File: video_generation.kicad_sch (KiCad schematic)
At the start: 49 parts, among them J12 28L22, J13 74LS86, J14 74LS166, J15 74LS161, K0000 74LS00, K10 74LS08, K11 74LS273, K12 74LS273, K14 74LS10, K15 74LS04, U14 74LS00, U2 74LS32, U3 74LS08, U4 74LS04, U5 74LS00

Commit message: video gen and memory: wire renaming, but something is still missing
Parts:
- added TP1: EXT, symbol Connector:TestPoint_Alt
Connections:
- net cl4 is gone; now on net ra4: E7E11.34 (RA4)
- net ~{BEAM} is gone; now on net BEAM: J?.5 (Pin_5)
- net GND: now also E12.8 (GND), H12H14.12 (GND), K11.10 (GND), K12.10 (GND), L10.8 (GND)
- net VCC: now also E12.1 (~{Mr}), E12.16 (VCC), H12H14.24 (VCC), K11.20 (VCC), K12.20 (VCC), L10.16 (VCC), R67.1
- net char0: now also H11.16 (Q6); no longer H11.2 (Q0)
- net char1: now also H11.2 (Q0); no longer H11.5 (Q1)
- net char2: now also H11.19 (Q7); no longer H11.6 (Q2)
- net char3: now also H11.12 (Q4); no longer H11.9 (Q3)
- net char4: now also H11.9 (Q3); no longer H11.12 (Q4)
- net char5: now also H11.6 (Q2); no longer H11.15 (Q5)
- net char6: now also H11.15 (Q5); no longer H11.16 (Q6)
- net char7: now also H11.5 (Q1); no longer H11.19 (Q7)
- net cl0: no longer E7E11.38 (RA0)
- net cl1: no longer E7E11.37 (RA1)
- net cl2: no longer E7E11.36 (RA2)
- net cl3: no longer E7E11.35 (RA3)
- net ra0: now reaches J12.1 (A0)
- net ra0: now also E7E11.38 (RA0)
- net ROM_D5: now reaches J12.12 (D5)
- net ROM_D5: now also K12.18 (D7)
- net ROM_D6: now reaches J12.13 (D6)
- net ROM_D6: now also K12.17 (D6)
- net ROM_D7: now reaches J12.14 (D7)
- net ROM_D7: now also K12.14 (D5)
- net ROM_A5: now reaches J12.17 (A5)
- net ROM_A5: now also K11.16 (Q6)
- net ROM_A6: now reaches J12.18 (A6)
- net ROM_A6: now also K11.19 (Q7)
- net ROM_A7: now reaches J12.19 (A7)
- net ROM_A7: now also K11.15 (Q5)
- net ra1: now reaches J12.2 (A1)
- net ra1: now also E7E11.37 (RA1)
- net ra2: now reaches J12.3 (A2)
- net ra2: now also E7E11.36 (RA2)
- net ra3: now reaches J12.4 (A3)
- net ra3: now also E7E11.35 (RA3)
- net ra4: now reaches J12.5 (A4)
- net A0: now reaches E7E11.24 (RS)
- net chmd3: now reaches H11.13 (D4)
- net chmd6: now reaches H11.14 (D5)
- net chmd0: now reaches H11.17 (D6)
- net chmd2: now reaches H11.18 (D7)
- net chmd1: now reaches H11.3 (D0)
- net chmd7: now reaches H11.4 (D1)
- net chmd5: now reaches H11.7 (D2)
- net chmd4: now reaches H11.8 (D3)
- net at K11.2 (Q0): now also TP1.1
- net 15MHzClock renamed PIXEL_CLK
- net MainClock renamed CRTC_CLK
- net attr_data0 renamed attrmd0
- net attr_data1 renamed attrmd1
- net attr_data2 renamed attrmd2
- net attr_data3 renamed attrmd3
- net attr_data4 renamed attrmd4
- net attr_data5 renamed attrmd5
- net attr_data6 renamed attrmd6
- net attr_data7 renamed attrmd7
- net data0 renamed D0
- net data1 renamed D1
- net data2 renamed D2
- net data3 renamed D3
- net data4 renamed D4
- net data5 renamed D5
- net data6 renamed D6
- net data7 renamed D7
- net ma0 renamed VMA0
- net ma1 renamed VMA1
- net ma10 renamed VMA10
- net ma2 renamed VMA2
- net ma3 renamed VMA3
- net ma4 renamed VMA4
- net ma5 renamed VMA5
- net ma6 renamed VMA6
- net ma7 renamed VMA7
- net ma8 renamed VMA8
- net ma9 renamed VMA9
- net ~{MainClock} renamed ~{CRTC_CLK}
- net ~{TC} renamed ~{PIXEL_EN}
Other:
- note added: "Attribute Memory Data"
- note added: "Character Memory Data"
- note added: "Raster address"
- note added: "TODO"
- note added: "Video memory Address"
- note removed: "D2 from attribute RAM is something related to cursor"
- note removed: "EXT pad"
- note removed: "NOTE:SWAP"
- note removed: "NOTE:SWAP: actual routing on board differs due to physical constraints, but functionality is the same."
- note removed: "ROM_A5"
- note removed: "ROM_A6"
- note removed: "ROM_A7"
- note removed: "ROM_D5"
- note removed: "ROM_D6"
- note removed: "ROM_D7"
- note removed: "VERIFY"
- note removed: "registered ATTR RAM D0"
- note removed: "registered ATTR RAM D1"
- note removed: "registered D2 attr ram"
- note removed: "registered D5 ROM"
- note removed: "registered D6 ROM"
- note removed: "registered D7 ROM"
- moved on the sheet: K10B, R42, R67

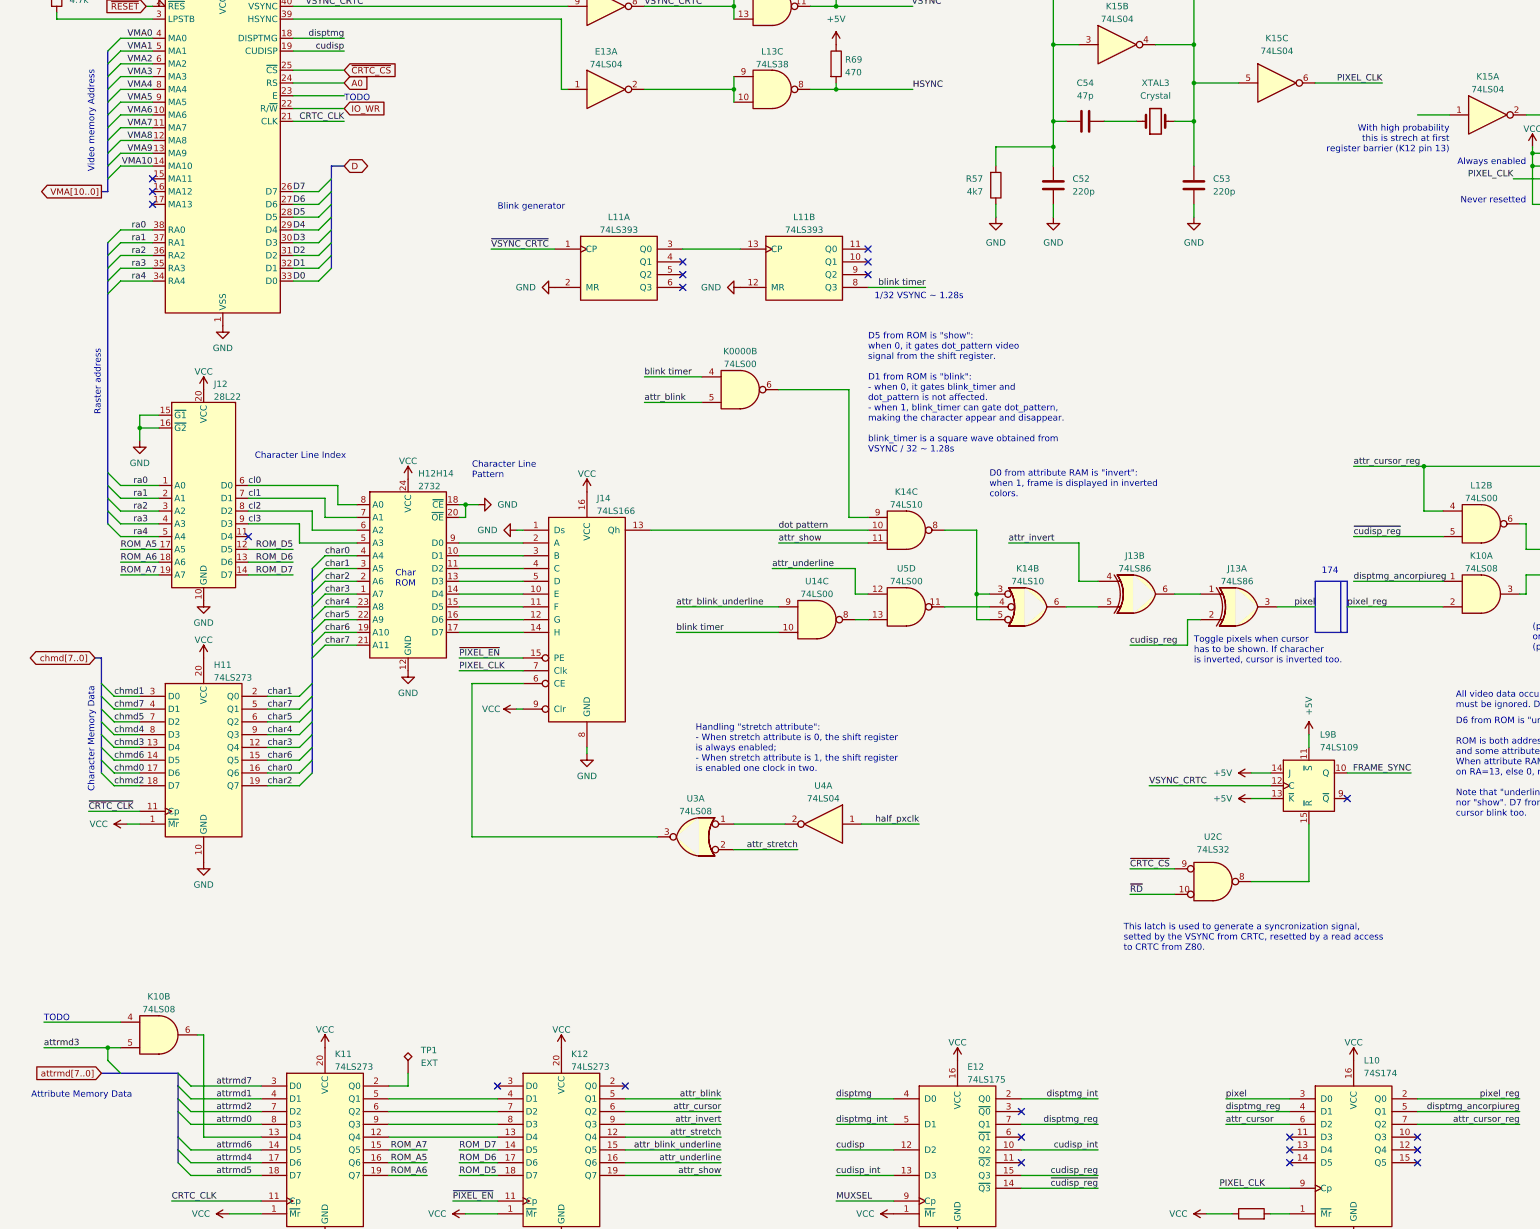
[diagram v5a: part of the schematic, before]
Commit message: Typo fixes
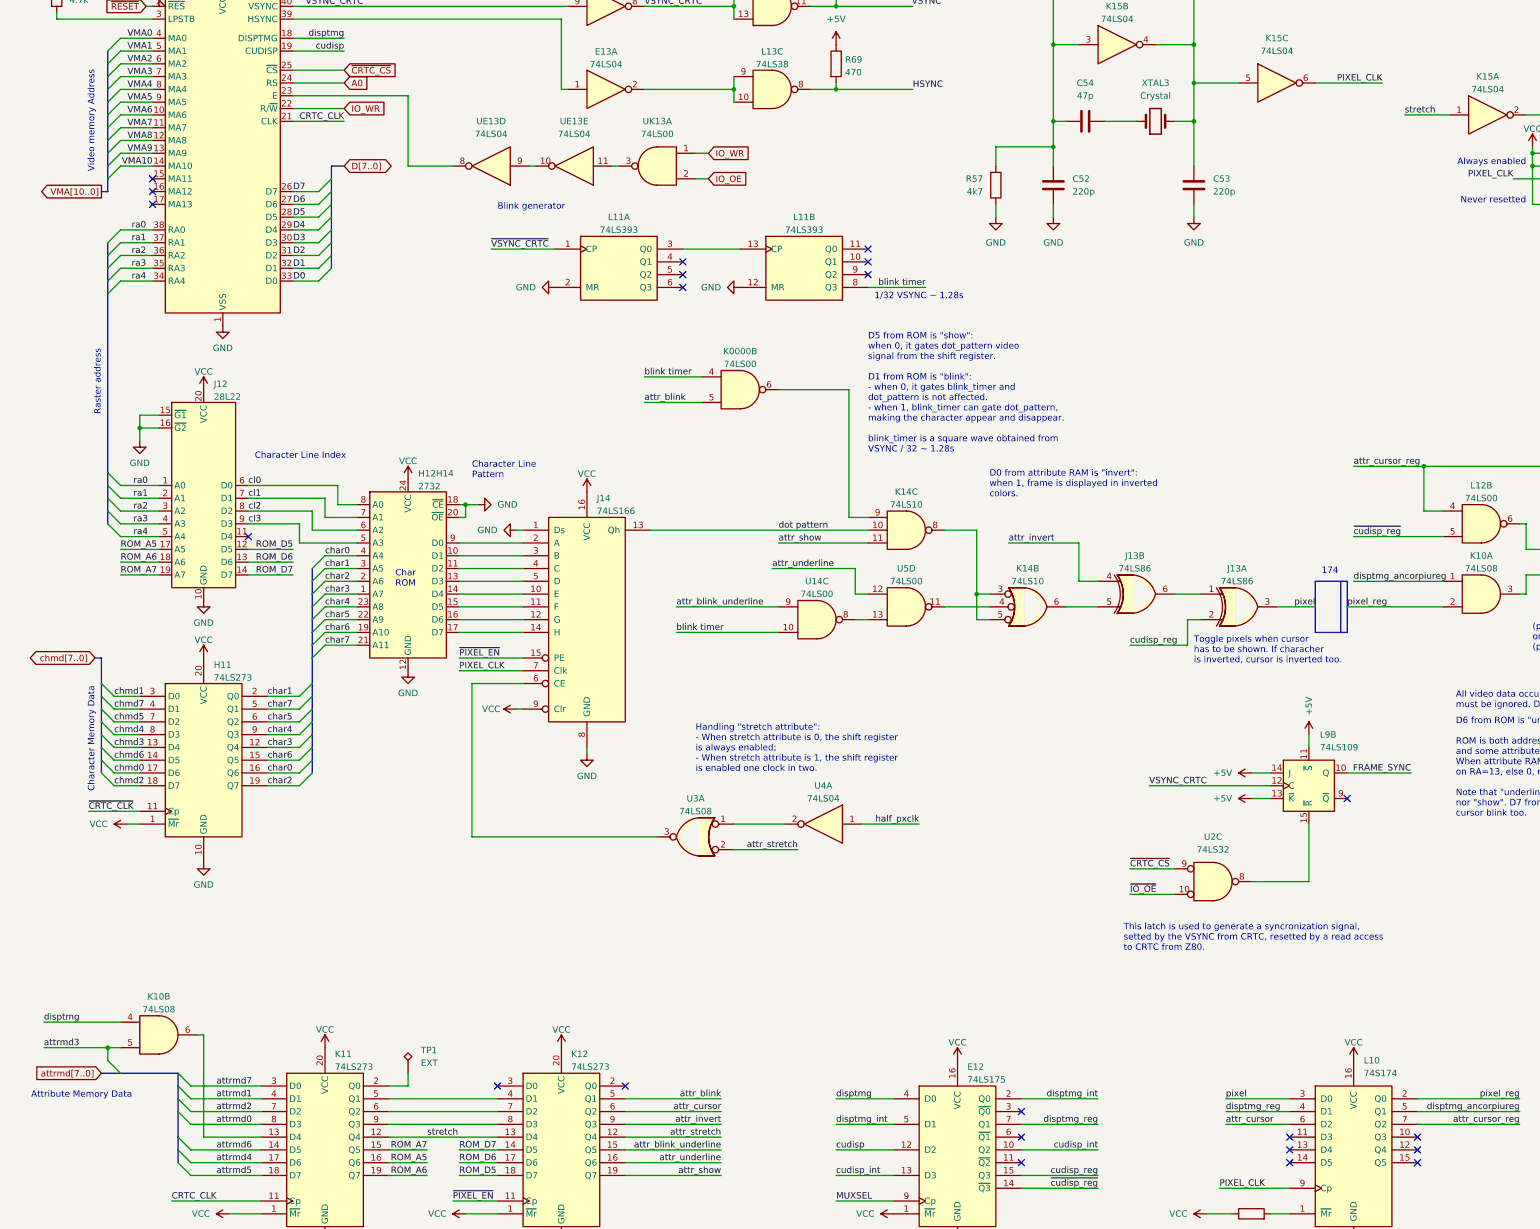
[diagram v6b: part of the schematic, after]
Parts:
- added UE13: 74LS04, symbol 74xx:74LS04
- added UK13: 74LS00, symbol 74xx:74LS38
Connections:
- net IO_WR: now also UK13.1
- net disptmg: now also K10.4
- net stretch: now reaches K11.12 (Q4), K12.13 (D4)
- net stretch: now also K15.1
- net at E7E11.23 (E): now also UE13.8
- net ~{RD} renamed ~{IO_OE}
- new net: UE13.11, UK13.3
- new net: UE13.10, UE13.9
- new net IO_OE: UK13.2
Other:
- note removed: "TODO"
- note removed: "With high probability this is strech at first register barrier (K12 pin 13)"
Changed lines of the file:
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@@
     (stroke (width 0) (type default))
   )
-  (wire (pts (xy 66.04 43.18) (xy 76.2 43.18))
+  (wire (pts (xy 66.04 43.18) (xy 88.9 43.18))
     (stroke (width 0) (type default))
   )
@@
     (stroke (width 0) (type default))
   )
+  (wire (pts (xy 88.9 57.15) (xy 97.79 57.15))
+    (stroke (width 0) (type default))
+  )
   (wire (pts (xy 365.76 39.37) (xy 365.76 44.45))
     (stroke (width 0) (type default))
@@
     (stroke (width 0) (type default))
   )
+  (wire (pts (xy 130.81 57.15) (xy 129.54 57.15))
+    (stroke (width 0) (type default))
+  )
   (wire (pts (xy 88.9 237.49) (xy 88.9 240.03))
     (stroke (width 0) (type default))
@@
     (stroke (width 0) (type default))
   )
-  (wire (pts (xy 289.56 46.99) (xy 295.91 46.99))
+  (wire (pts (xy 287.02 46.99) (xy 295.91 46.99))
     (stroke (width 0) (type default))
   )
@@
     (stroke (width 0) (type default))
   )
+  (wire (pts (xy 88.9 43.18) (xy 88.9 57.15))
+    (stroke (width 0) (type default))
+  )
   (wire (pts (xy 250.19 260.35) (xy 264.16 260.35))
     (stroke (width 0) (type default))
@@
     (stroke (width 0) (type default))
   )
+  (wire (pts (xy 148.59 59.69) (xy 146.05 59.69))
+    (stroke (width 0) (type default))
+  )
   (wire (pts (xy 30.48 172.72) (xy 35.56 172.72))
     (stroke (width 0) (type default))
@@
     (stroke (width 0) (type default))
   )
+  (wire (pts (xy 148.59 54.61) (xy 146.05 54.61))
+    (stroke (width 0) (type default))
+  )
   (wire (pts (xy 85.09 247.65) (xy 106.68 247.65))
     (stroke (width 0) (type default))
@@
     (stroke (width 0) (type default))
   )
+  (wire (pts (xy 114.3 57.15) (xy 113.03 57.15))
+    (stroke (width 0) (type default))
+  )
   (wire (pts (xy 251.46 247.65) (xy 264.16 247.65))
     (stroke (width 0) (type default))
@@
     (effects (font (size 1.27 1.27)) (justify left bottom))
   )
-  (text "TODO" (at 16.51 227.33 0)
-    (effects (font (size 1.27 1.27)) (justify left bottom))
-  )
   (text "Pixel clock generator" (at 203.2 16.51 0)
     (effects (font (size 1.27 1.27)) (justify left bottom))
@@
     (effects (font (size 1.27 1.27)) (justify left bottom))
   )
-  (text "TODO" (at 76.2 44.45 0)
-    (effects (font (size 1.27 1.27)) (justify left bottom))
-  )
   (text "Video memory Address" (at 26.67 58.42 90)
     (effects (font (size 1.27 1.27)) (justify left bottom))
@@
     (effects (font (size 1.27 1.27)) (justify left bottom))
   )
-  (text "With high probability\nthis is strech at first\nregister barrier (K12 pin 13)"
-    (at 295.91 54.61 0)
-    (effects (font (size 1.27 1.27)) (justify right bottom))
-  )
   (text "Handling \"stretch attribute\":\n- When stretch attribute is 0, the shift register\nis always enabled;\n- When stretch attribute is 1, the shift register\nis enabled one clock in two."
     (at 146.05 177.8 0)
@@
     (effects (font (size 1.27 1.27)) (justify right bottom))
   )
+  (label "stretch" (at 92.71 250.19 0) (fields_autoplaced)
+    (effects (font (size 1.27 1.27)) (justify left bottom))
+  )
   (label "cudisp" (at 76.2 34.29 180) (fields_autoplaced)
     (effects (font (size 1.27 1.27)) (justify right bottom))
@@
     (effects (font (size 1.27 1.27)) (justify right bottom))
   )
-  (label "~{RD}" (at 232.41 201.93 0) (fields_autoplaced)
+  (label "~{IO_OE}" (at 232.41 201.93 0) (fields_autoplaced)
     (effects (font (size 1.27 1.27)) (justify left bottom))
   )
@@
     (effects (font (size 1.27 1.27)) (justify left bottom))
   )
+  (label "disptmg" (at 16.51 227.33 0) (fields_autoplaced)
+    (effects (font (size 1.27 1.27)) (justify left bottom))
+  )
   (label "pixel" (at 269.24 144.78 180) (fields_autoplaced)
     (effects (font (size 1.27 1.27)) (justify right bottom))
@@
     (effects (font (size 1.27 1.27)) (justify right bottom))
   )
+  (label "stretch" (at 287.02 46.99 0) (fields_autoplaced)
+    (effects (font (size 1.27 1.27)) (justify left bottom))
+  )
   (label "ROM_D5" (at 99.06 257.81 0) (fields_autoplaced)
     (effects (font (size 1.27 1.27)) (justify left bottom))
@@
     (effects (font (size 1.27 1.27)) (justify right bottom))
   )
+  (global_label "IO_OE" (shape input) (at 148.59 59.69 0) (fields_autoplaced)
+    (effects (font (size 1.27 1.27)) (justify left))
+    (property "Intersheetrefs" "${INTERSHEET_REFS}" (at 156.9576 59.69 0)
+      (effects (font (size 1.27 1.27)) (justify left) hide)
+    )
+  )
   (global_label "attrmd[7..0]" (shape input) (at 27.94 237.49 180) (fields_autoplaced)
     (effects (font (size 1.27 1.27)) (justify right))
@@
     )
   )
+  (global_label "IO_WR" (shape input) (at 148.59 54.61 0) (fields_autoplaced)
+    (effects (font (size 1.27 1.27)) (justify left))
+    (property "Intersheetrefs" "${INTERSHEET_REFS}" (at 157.1995 54.61 0)
+      (effects (font (size 1.27 1.27)) (justify left) hide)
+    )
+  )
   (global_label "IO_WR" (shape input) (at 76.2 45.72 0) (fields_autoplaced)
     (effects (font (size 1.27 1.27)) (justify left))
@@
     )
   )
-  (global_label "D" (shape bidirectional) (at 76.2 57.15 0) (fields_autoplaced)
+  (global_label "D[7..0]" (shape bidirectional) (at 76.2 57.15 0) (fields_autoplaced)
     (effects (font (size 1.27 1.27)) (justify left))
-    (property "Intersheetrefs" "${INTERSHEET_REFS}" (at 81.5665 57.15 0)
+    (property "Intersheetrefs" "${INTERSHEET_REFS}" (at 86.8885 57.15 0)
       (effects (font (size 1.27 1.27)) (justify left) hide)
     )
@@
     )
   )
+  (symbol (lib_id "74xx:74LS38") (at 138.43 57.15 0) (mirror y) (unit 1)
+    (in_bom yes) (on_board yes) (dnp no) (fields_autoplaced)
+    (property "Reference" "UK13" (at 138.4383 48.26 0)
+      (effects (font (size 1.27 1.27)))
+    )
+    (property "Value" "74LS00" (at 138.4383 50.8 0)
+      (effects (font (size 1.27 1.27)))
+    )
+    (property "Footprint" "" (at 138.43 57.15 0)
+      (effects (font (size 1.27 1.27)) hide)
+    )
+    (property "Datasheet" "http://www.ti.com/lit/gpn/sn74LS38" (at 138.43 57.15 0)
+      (effects (font (size 1.27 1.27)) hide)
+    )
+    (property "Datasheet" "http://www.ti.com/lit/gpn/sn74LS38" (at 181.61 -3.81 0)
+      (effects (font (size 1.27 1.27)) hide)
+    )
+    (pin "1")
+    (pin "2")
+    (pin "3")
+    (pin "4")
+    (pin "5")
+    (pin "6")
+    (pin "10")
+    (pin "8")
+    (pin "9")
+    (pin "11")
+    (pin "12")
+    (pin "13")
+    (pin "14")
+    (pin "7")
+    (instances
+      (project "ceda"
+        (path "/12a6dbe3-008d-4c5b-88f6-9f1c816060be/ce60e45b-d802-4380-8f39-bef3de5fa20e"
+          (reference "UK13") (unit 1)
+        )
+      )
+    )
+  )
   (symbol (lib_id "74xx:74LS32") (at 248.92 199.39 0) (unit 3) (convert 2)
     (in_bom yes) (on_board yes) (dnp no) (fields_autoplaced)
@@
     )
   )
+  (symbol (lib_id "74xx:74LS04") (at 105.41 57.15 180) (unit 4)
+    (in_bom yes) (on_board yes) (dnp no) (fields_autoplaced)
+    (property "Reference" "UE13" (at 105.41 48.26 0)
+      (effects (font (size 1.27 1.27)))
+    )
+    (property "Value" "74LS04" (at 105.41 50.8 0)
+      (effects (font (size 1.27 1.27)))
+    )
+    (property "Footprint" "" (at 105.41 57.15 0)
+      (effects (font (size 1.27 1.27)) hide)
+    )
+    (property "Datasheet" "http://www.ti.com/lit/gpn/sn74LS04" (at 105.41 57.15 0)
+      (effects (font (size 1.27 1.27)) hide)
+    )
+    (pin "1")
+    (pin "2")
+    (pin "3")
+    (pin "4")
+    (pin "5")
+    (pin "6")
+    (pin "8")
+    (pin "9")
+    (pin "10")
+    (pin "11")
+    (pin "12")
+    (pin "13")
+    (pin "14")
+    (pin "7")
+    (instances
+      (project "ceda"
+        (path "/12a6dbe3-008d-4c5b-88f6-9f1c816060be/ce60e45b-d802-4380-8f39-bef3de5fa20e"
+          (reference "UE13") (unit 4)
+        )
+      )
+    )
+  )
   (symbol (lib_id "power:GND") (at 52.07 88.9 0) (unit 1)
     (in_bom yes) (on_board yes) (dnp no) (fields_autoplaced)
@@
         )
       )
+    )
+  )
+  (symbol (lib_id "74xx:74LS04") (at 121.92 57.15 180) (unit 5)
+    (in_bom yes) (on_board yes) (dnp no) (fields_autoplaced)
+    (property "Reference" "UE13" (at 121.92 48.26 0)
+      (effects (font (size 1.27 1.27)))
+    )
+    (property "Value" "74LS04" (at 121.92 50.8 0)
+      (effects (font (size 1.27 1.27)))
+    )
+    (property "Footprint" "" (at 121.92 57.15 0)
+      (effects (font (size 1.27 1.27)) hide)
+    )
+    (property "Datasheet" "http://www.ti.com/lit/gpn/sn74LS04" (at 121.92 57.15 0)
+      (effects (font (size 1.27 1.27)) hide)
+    )
+    (pin "1")
+    (pin "2")
+    (pin "3")
+    (pin "4")
+    (pin "5")
+    (pin "6")
+    (pin "8")
+    (pin "9")
+    (pin "10")
+    (pin "11")
+    (pin "12")
+    (pin "13")
+    (pin "14")
+    (pin "7")
+    (instances
+      (project "ceda"
+        (path "/12a6dbe3-008d-4c5b-88f6-9f1c816060be/ce60e45b-d802-4380-8f39-bef3de5fa20e"
+          (reference "UE13") (unit 5)
+        )
+      )

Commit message: Fixed typo in video generation. Added some useful (I hope) notes.
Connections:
- net MUXSEL is gone; now on net ~{CRTC_CLK}: E12.9 (Cp)
- net BEAM: no longer J?.5 (Pin_5)
- net CRTC_CLK: no longer K11.11 (Cp)
- net GND: now also J?.1 (Pin_1), J?.9 (Pin_9)
- net ~{CRTC_CLK}: now also K11.11 (Cp)
- net ~{pixel_cursor}: now reaches L12.11, L13.4, L13.5
- net ~{pixel_cursor}: now also J?.6 (Pin_6)
- net pixel_valid: now reaches K10.3, L12.13, L12.2
- net pixel_valid: now also J?.5 (Pin_5)
- no-connect marks 27 -> 23
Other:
- note added: "All RAMs outputs (both char and attr) are syncronized on negative edge of CRTC_CLK."
- note added: "Both disptmg and cudisp must be delayed to be in sync with the pipeline. At the output of J14, a double CRTC_CLK delay is needed."
- note added: "Last stage of pipeline: pixel is registered. To keep signals in sync with the pipeline, the signals used in this last stage are delayed. Why cudisp is not delayed? We don't know."
- note added: "Then, character is sampled for each character in xx shift register. Attributes are sampled for each character in register K12. Note: ~{PIXEL_EN} period is doubled when horizontal stretch is requested. For this reason both attributes and character must be freezed with PIXEL_EN."
- moved on the sheet: J?, R75

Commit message: Components renaming according to the Uxy convention.
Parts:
- UL12: renamed from L12; value 74LS00 -> 74S00
- renumbered E12 to UE12, E13 to UE13, E7E11 to UE7, U3 to UF13, H11 to UH11, H12H14 to UH12, J12 to UJ12, J13 to UJ13, J14 to UJ14, J15 to UJ15, K10 to UK10, K11 to UK11, K12 to UK12, K0000 to UK13, U5 to UK13, U14 to UK13, K14 to UK14, K15 to UK15, U4 to UK15, L10 to UL10, L11 to UL11, L13 to UL13
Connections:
- net VSYNC: now also R68.2, UL13.11
- net cudisp_reg: now also UJ13.10; no longer UJ13.2
- net half_pxclk: now also UK15.13; no longer UK15.1
- net pixel: now also UJ13.8; no longer UJ13.3
- net at UJ13.6: now also UJ13.9; no longer UJ13.1
- net at UF13.1: now also UK15.12; no longer UK15.2
- net at UE7.23 (E): now also UE13.10; no longer UE13.8
- net at UK13.3: now also UE13.13; no longer UE13.11
- new net: UE13.11, UE13.12
